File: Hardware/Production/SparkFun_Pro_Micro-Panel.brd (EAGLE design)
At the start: 103.6 x 148.6 mm, 1548 parts, among them J1 Qwiic, J13 Qwiic, J17 Qwiic, J2 Qwiic, J21 Qwiic, J25 Qwiic, J29 Qwiic, J33 Qwiic, J37 Qwiic, J41 Qwiic, J45 Qwiic, J49 Qwiic, J53 Qwiic, J57 Qwiic, J9 Qwiic, U1 3.3V, U10 3.3V, U11 ATmega32U4, U12 3.3V, U13 ATmega32U4, U14 3.3V, U15 ATmega32U4, U16 3.3V, U17 ATmega32U4, U18 3.3V, U19 ATmega32U4, U2 ATmega32U4, U20 3.3V, U21 ATmega32U4, U22 3.3V, U23 ATmega32U4, U24 3.3V, U25 ATmega32U4, U26 3.3V, U27 ATmega32U4, U28 3.3V, U29 ATmega32U4, U3 ATmega32U4, U30 3.3V, U4 3.3V, U5 ATmega32U4, U6 3.3V, U7 ATmega32U4, U8 3.3V, U9 ATmega32U4, Y1 32MHz, Y10 32MHz, Y11 32MHz, Y12 32MHz, Y13 32MHz, Y14 32MHz, Y15 32MHz, Y2 32MHz, Y3 32MHz, Y4 32MHz, Y5 32MHz, Y6 32MHz, Y7 32MHz, Y8 32MHz, Y9 32MHz

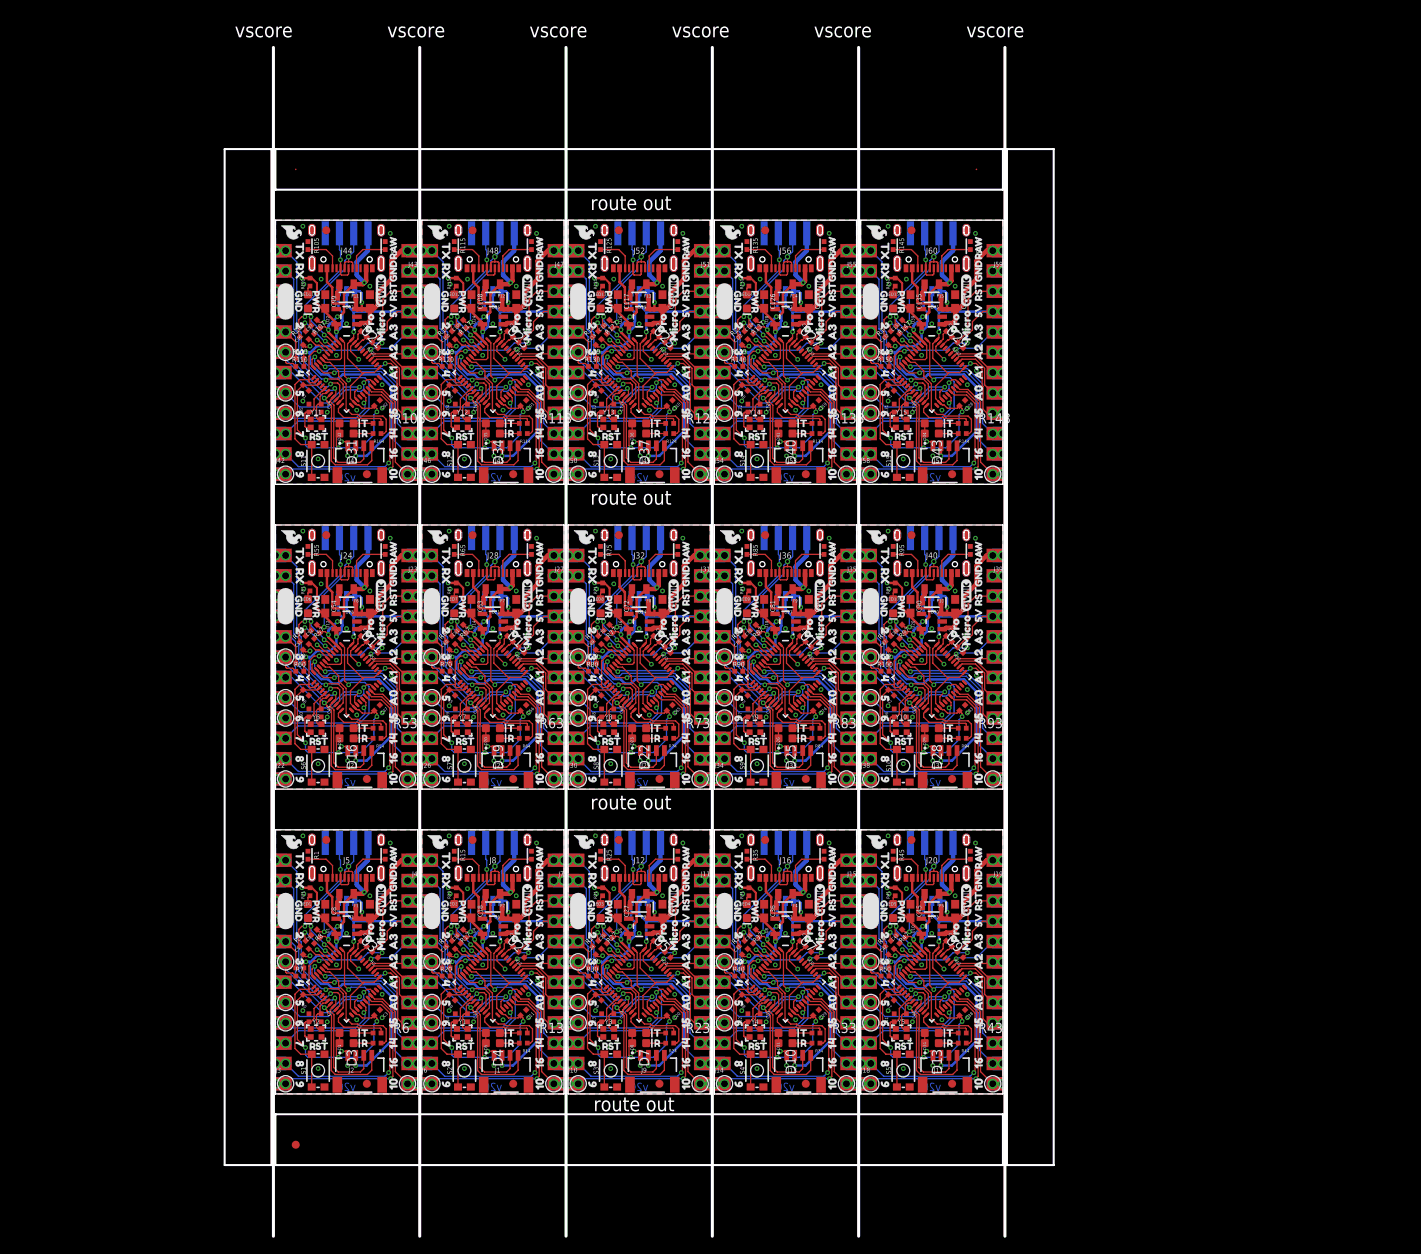
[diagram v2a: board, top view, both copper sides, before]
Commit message: Red boards ordered
Modify castellated 1x12 to larger diameter plated castellated holes. Panelize with route-out around castellated edges. Scoot Qwiic connector in to use that side of the board as the tab.
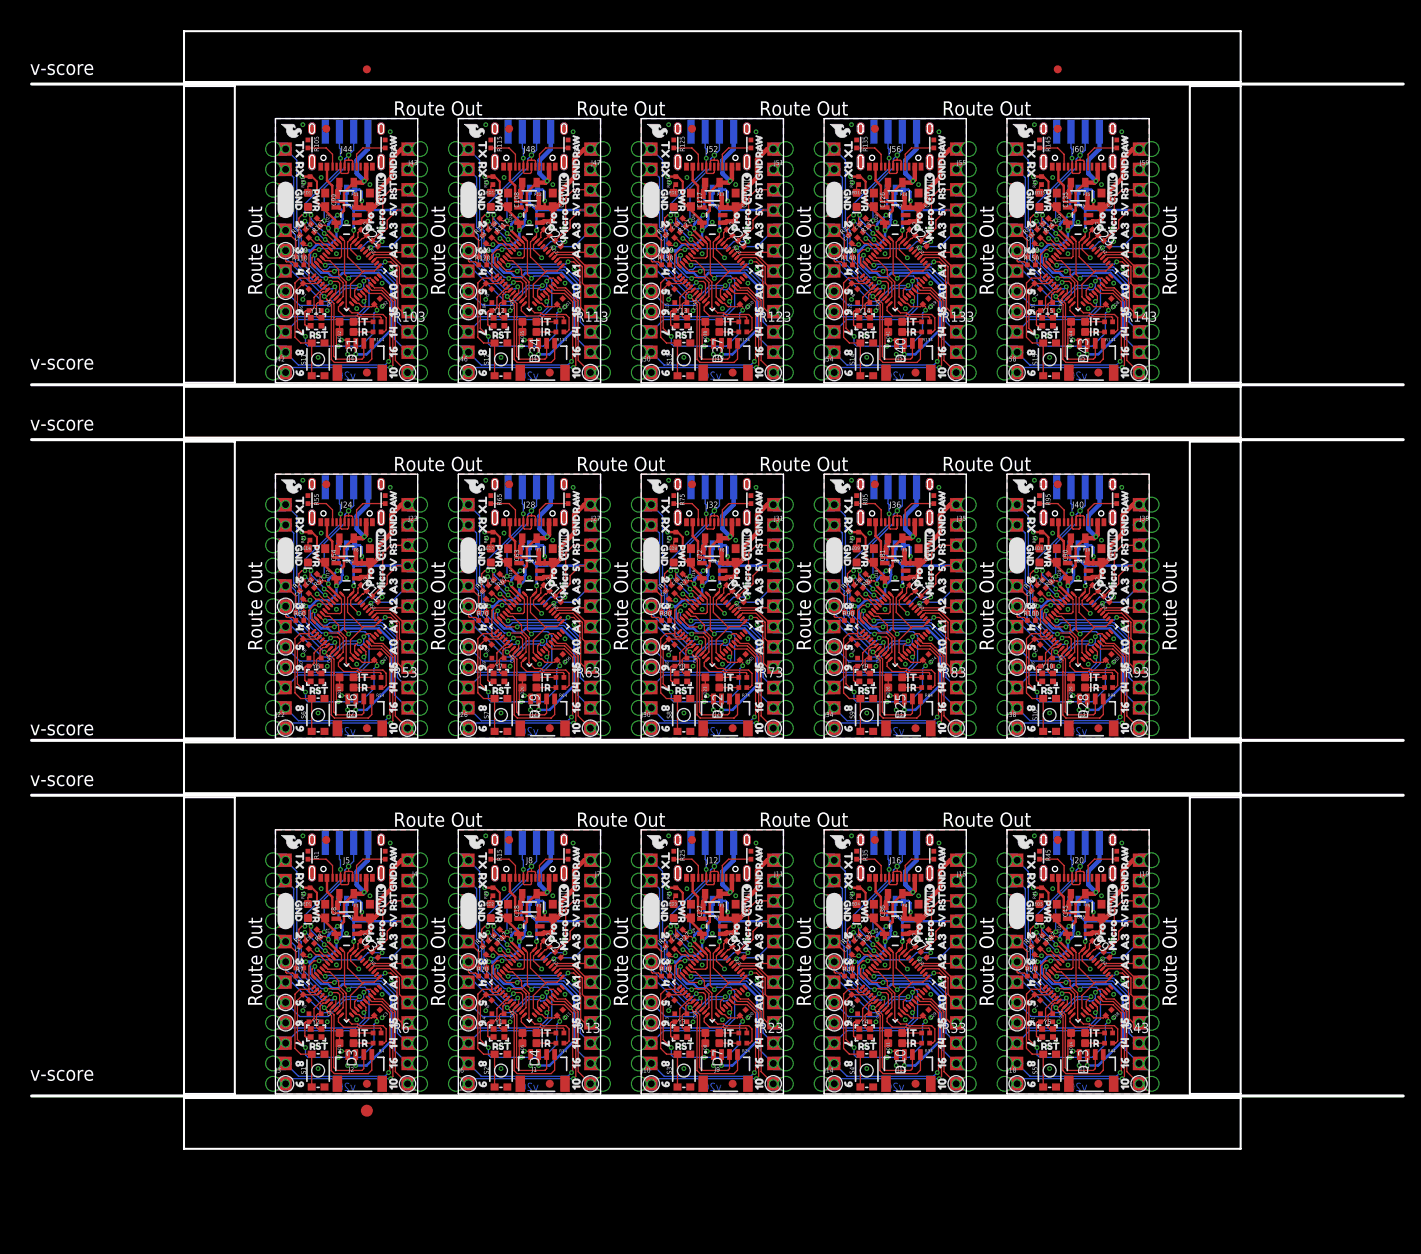
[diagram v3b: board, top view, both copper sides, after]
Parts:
- E$2: device SparkFun-Aesthetics:FIDUCIAL-0.2MM -> SparkFun-Aesthetics:FIDUCIAL-1X2
- E$3: device SparkFun-Aesthetics:FIDUCIAL-0.2MM -> SparkFun-Retired:FIDUCIAL-1.5X3
- moved E$3 140.2 mm to (11.4, -2.10)
- moved E$1 134.7 mm to (11.4, 128.1)
- moved E$2 96.1 mm to (97.8, 128.1)
- moved J57 22.3 mm to (102.0, 93.8)
- moved C129 22.3 mm to (102.5, 107.7)
- moved C133 22.3 mm to (96.6, 108.1)
- moved C134 22.3 mm to (103.3, 111.8)
- moved JP57 22.3 mm to (102.9, 90.2)
- moved JP58 22.3 mm to (97.8, 120.7)
- moved LED15 22.3 mm to (95.5, 111.8)
- moved R145 22.3 mm to (95.5, 118.7)
- moved R146 22.3 mm to (105.2, 118.7)
- moved R147 22.3 mm to (96.3, 109.1)
- moved U$888 22.3 mm to (103.3, 106.9)
- moved U$903 22.3 mm to (94.4, 114.0)
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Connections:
- new net 3.3V12: C117.2, J49.2, JP52.1, R121.2, R129.2, R130.2, U26.5
- new net 3.3V13: C126.2, J53.2, JP56.1, R131.2, R139.2, R140.2, U28.5
- new net 3.3V14: C135.2, J57.2, JP60.1, R141.2, R149.2, R150.2, U30.5
- new net 3.3V2: C27.2, J9.2, JP11.1, R21.2, R29.2, R30.2, U6.5
- new net 3.3V3: C36.2, J13.2, JP16.1, R31.2, R39.2, R40.2, U8.5
- new net 3.3V4: C45.2, J17.2, JP20.1, R41.2, R49.2, R50.2, U10.5
- new net 3.3V7: C72.2, J29.2, JP32.1, R71.2, R79.2, R80.2, U16.5
- new net 3.3V8: C81.2, J33.2, JP36.1, R81.2, R89.2, R90.2, U18.5
- new net 3.3V9: C90.2, J37.2, JP40.1, R100.2, R91.2, R99.2, U20.5
- new net A10: J11.7, J11.7B, U5.37
- new net A11: J11.8, J11.8B, U5.36
- new net A12: J15.5, J15.5B, U7.39
- new net A13: J15.6, J15.6B, U7.38
- new net A14: J15.7, J15.7B, U7.37
- new net A15: J15.8, J15.8B, U7.36
- new net A16: J19.5, J19.5B, U9.39
- new net A17: J19.6, J19.6B, U9.38
- new net A18: J19.7, J19.7B, U9.37
- new net A19: J19.8, J19.8B, U9.36
- new net A28: J31.5, J31.5B, U15.39
- new net A29: J31.6, J31.6B, U15.38
- new net A30: J31.7, J31.7B, U15.37
- new net A31: J31.8, J31.8B, U15.36
- new net A32: J35.5, J35.5B, U17.39
- new net A33: J35.6, J35.6B, U17.38
- new net A34: J35.7, J35.7B, U17.37
- new net A35: J35.8, J35.8B, U17.36
- new net A36: J39.5, J39.5B, U19.39
- new net A37: J39.6, J39.6B, U19.38
- new net A38: J39.7, J39.7B, U19.37
- new net A39: J39.8, J39.8B, U19.36
- new net A48: J51.5, J51.5B, U25.39
- new net A49: J51.6, J51.6B, U25.38
- new net A50: J51.7, J51.7B, U25.37
- new net A51: J51.8, J51.8B, U25.36
- new net A52: J55.5, J55.5B, U27.39
- new net A53: J55.6, J55.6B, U27.38
- new net A54: J55.7, J55.7B, U27.37
- new net A55: J55.8, J55.8B, U27.36
- new net A56: J59.5, J59.5B, U29.39
- new net A57: J59.6, J59.6B, U29.38
- new net A58: J59.7, J59.7B, U29.37
- new net A59: J59.8, J59.8B, U29.36
- new net A8: J11.5, J11.5B, U5.39
- new net A9: J11.6, J11.6B, U5.38
- new net AREF12: C111.2, U25.42
- new net AREF13: C120.2, U27.42
- new net AREF14: C129.2, U29.42
- new net AREF2: C21.2, U5.42
- new net AREF3: C30.2, U7.42
- new net AREF4: C39.2, U9.42
- new net AREF7: C66.2, U15.42
- new net AREF8: C75.2, U17.42
- new net AREF9: C84.2, U19.42
- new net D+12: R128.2, U25.4
- new net D+13: R138.2, U27.4
- new net D+14: R148.2, U29.4
- new net D+2: R28.2, U5.4
- new net D+3: R38.2, U7.4
- new net D+4: R48.2, U9.4
- new net D+7: R78.2, U15.4
- new net D+8: R88.2, U17.4
- new net D+9: R98.2, U19.4
- new net D-12: R127.2, U25.3
- new net D-13: R137.2, U27.3
- new net D-14: R147.2, U29.3
- new net D-2: R27.2, U5.3
- new net D-3: R37.2, U7.3
- new net D-4: R47.2, U9.3
- new net D-7: R77.2, U15.3
- new net D-8: R87.2, U17.3
- new net D-9: R97.2, U19.3
- new net D-_HV12: J52.A7, J52.B7, JP51.D-, R127.1
- new net D-_HV13: J56.A7, J56.B7, JP55.D-, R137.1
- new net D-_HV14: J60.A7, J60.B7, JP59.D-, R147.1
- new net D-_HV2: J12.A7, J12.B7, JP10.D-, R27.1
- new net D-_HV3: J16.A7, J16.B7, JP15.D-, R37.1
- new net D-_HV4: J20.A7, J20.B7, JP19.D-, R47.1
- new net D-_HV7: J32.A7, J32.B7, JP31.D-, R77.1
- new net D-_HV8: J36.A7, J36.B7, JP35.D-, R87.1
- new net D-_HV9: J40.A7, J40.B7, JP39.D-, R97.1
- new net D100: J58.2, J58.2B, U29.28
- new net D101: J58.6, J58.6B, U29.25
- new net D102: J58.5, J58.5B, U29.31
- new net D103: J58.4, J58.4B, U29.27
- new net D104: J58.3, J58.3B, U29.1
- new net D105: J59.12, J59.12B, U29.30
- new net D15: J10.1, J10.1B, U5.29
- new net D16: J10.2, J10.2B, U5.28
- new net D17: J10.6, J10.6B, U5.25
- new net D18: J10.5, J10.5B, U5.31
- new net D19: J10.4, J10.4B, U5.27
- new net D2/SDA12: J49.3, J50.8, J50.8B, R129.1, U25.19
- new net D2/SDA13: J53.3, J54.8, J54.8B, R139.1, U27.19
- new net D2/SDA14: J57.3, J58.8, J58.8B, R149.1, U29.19
- new net D2/SDA2: J10.8, J10.8B, J9.3, R29.1, U5.19
- new net D2/SDA3: J13.3, J14.8, J14.8B, R39.1, U7.19
- new net D2/SDA4: J17.3, J18.8, J18.8B, R49.1, U9.19
- new net D2/SDA7: J29.3, J30.8, J30.8B, R79.1, U15.19
- new net D2/SDA8: J33.3, J34.8, J34.8B, R89.1, U17.19
- new net D2/SDA9: J37.3, J38.8, J38.8B, R99.1, U19.19
- new net D20: J10.3, J10.3B, U5.1
- new net D21: J11.12, J11.12B, U5.30
- new net D22: J14.1, J14.1B, U7.29
- new net D23: J14.2, J14.2B, U7.28
- new net D24: J14.6, J14.6B, U7.25
- new net D25: J14.5, J14.5B, U7.31
- new net D26: J14.4, J14.4B, U7.27
- new net D27: J14.3, J14.3B, U7.1
- new net D28: J15.12, J15.12B, U7.30
- new net D29: J18.1, J18.1B, U9.29
- new net D3/SCL12: J49.4, J50.7, J50.7B, R130.1, U25.18
- new net D3/SCL13: J53.4, J54.7, J54.7B, R140.1, U27.18
- new net D3/SCL14: J57.4, J58.7, J58.7B, R150.1, U29.18
- new net D3/SCL2: J10.7, J10.7B, J9.4, R30.1, U5.18
- new net D3/SCL3: J13.4, J14.7, J14.7B, R40.1, U7.18
- new net D3/SCL4: J17.4, J18.7, J18.7B, R50.1, U9.18
- new net D3/SCL7: J29.4, J30.7, J30.7B, R80.1, U15.18
- new net D3/SCL8: J33.4, J34.7, J34.7B, R90.1, U17.18
- new net D3/SCL9: J37.4, J38.7, J38.7B, R100.1, U19.18
- new net D30: J18.2, J18.2B, U9.28
- new net D31: J18.6, J18.6B, U9.25
- new net D32: J18.5, J18.5B, U9.31
- new net D33: J18.4, J18.4B, U9.27
- new net D34: J18.3, J18.3B, U9.1
- new net D35: J19.12, J19.12B, U9.30
- new net D50: J30.1, J30.1B, U15.29
- new net D51: J30.2, J30.2B, U15.28
- new net D52: J30.6, J30.6B, U15.25
- new net D53: J30.5, J30.5B, U15.31
- new net D54: J30.4, J30.4B, U15.27
- new net D55: J30.3, J30.3B, U15.1
- new net D56: J31.12, J31.12B, U15.30
- new net D57: J34.1, J34.1B, U17.29
- new net D58: J34.2, J34.2B, U17.28
- new net D59: J34.6, J34.6B, U17.25
- new net D60: J34.5, J34.5B, U17.31
- new net D61: J34.4, J34.4B, U17.27
- new net D62: J34.3, J34.3B, U17.1
- new net D63: J35.12, J35.12B, U17.30
- new net D64: J38.1, J38.1B, U19.29
- new net D65: J38.2, J38.2B, U19.28
- new net D66: J38.6, J38.6B, U19.25
- new net D67: J38.5, J38.5B, U19.31
- new net D68: J38.4, J38.4B, U19.27
- new net D69: J38.3, J38.3B, U19.1
- new net D70: J39.12, J39.12B, U19.30
- new net D85: J50.1, J50.1B, U25.29
- new net D86: J50.2, J50.2B, U25.28
- new net D87: J50.6, J50.6B, U25.25
- new net D88: J50.5, J50.5B, U25.31
- new net D89: J50.4, J50.4B, U25.27
- new net D90: J50.3, J50.3B, U25.1
- new net D91: J51.12, J51.12B, U25.30
- new net D92: J54.1, J54.1B, U27.29
- new net D93: J54.2, J54.2B, U27.28
- new net D94: J54.6, J54.6B, U27.25
- new net D95: J54.5, J54.5B, U27.31
- new net D96: J54.4, J54.4B, U27.27
- new net D97: J54.3, J54.3B, U27.1
- new net D98: J55.12, J55.12B, U27.30
- new net D99: J58.1, J58.1B, U29.29
- new net DP_HV12: J52.A6, J52.B6, JP51.D+, R128.1
- new net DP_HV13: J56.A6, J56.B6, JP55.D+, R138.1
- new net DP_HV14: J60.A6, J60.B6, JP59.D+, R148.1
- new net DP_HV2: J12.A6, J12.B6, JP10.D+, R28.1
- new net DP_HV3: J16.A6, J16.B6, JP15.D+, R38.1
- new net DP_HV4: J20.A6, J20.B6, JP19.D+, R48.1
- new net DP_HV7: J32.A6, J32.B6, JP31.D+, R78.1
- new net DP_HV8: J36.A6, J36.B6, JP35.D+, R88.1
- new net DP_HV9: J40.A6, J40.B6, JP39.D+, R98.1
- new net GND12: C109.1, C110.1, C111.1, C112.2, C113.2, C114.1, C115.1, C116.1, C117.1, J49.1, J50.10, J50.10B, J50.9, J50.9B, J51.2, J51.2B, J52.GND, J52.GND2, JP51.GND, LED13.C, R125.1, R126.1, S13.1, S13.2, U25.15, U25.23, U25.33, U25.35, U25.43, U25.5, U26.2
- new net GND13: C118.1, C119.1, C120.1, C121.2, C122.2, C123.1, C124.1, C125.1, C126.1, J53.1, J54.10, J54.10B, J54.9, J54.9B, J55.2, J55.2B, J56.GND, J56.GND2, JP55.GND, LED14.C, R135.1, R136.1, S14.1, S14.2, U27.15, U27.23, U27.33, U27.35, U27.43, U27.5, U28.2
- new net GND14: C127.1, C128.1, C129.1, C130.2, C131.2, C132.1, C133.1, C134.1, C135.1, J57.1, J58.10, J58.10B, J58.9, J58.9B, J59.2, J59.2B, J60.GND, J60.GND2, JP59.GND, LED15.C, R145.1, R146.1, S15.1, S15.2, U29.15, U29.23, U29.33, U29.35, U29.43, U29.5, U30.2
- new net GND2: C19.1, C20.1, C21.1, C22.2, C23.2, C24.1, C25.1, C26.1, C27.1, J10.10, J10.10B, J10.9, J10.9B, J11.2, J11.2B, J12.GND, J12.GND2, J9.1, JP10.GND, LED3.C, R25.1, R26.1, S3.1, S3.2, U5.15, U5.23, U5.33, U5.35, U5.43, U5.5, U6.2
- new net GND3: C28.1, C29.1, C30.1, C31.2, C32.2, C33.1, C34.1, C35.1, C36.1, J13.1, J14.10, J14.10B, J14.9, J14.9B, J15.2, J15.2B, J16.GND, J16.GND2, JP15.GND, LED4.C, R35.1, R36.1, S4.1, S4.2, U7.15, U7.23, U7.33, U7.35, U7.43, U7.5, U8.2
- new net GND4: C37.1, C38.1, C39.1, C40.2, C41.2, C42.1, C43.1, C44.1, C45.1, J17.1, J18.10, J18.10B, J18.9, J18.9B, J19.2, J19.2B, J20.GND, J20.GND2, JP19.GND, LED5.C, R45.1, R46.1, S5.1, S5.2, U10.2, U9.15, U9.23, U9.33, U9.35, U9.43, U9.5
- new net GND7: C64.1, C65.1, C66.1, C67.2, C68.2, C69.1, C70.1, C71.1, C72.1, J29.1, J30.10, J30.10B, J30.9, J30.9B, J31.2, J31.2B, J32.GND, J32.GND2, JP31.GND, LED8.C, R75.1, R76.1, S8.1, S8.2, U15.15, U15.23, U15.33, U15.35, U15.43, U15.5, U16.2
- new net GND8: C73.1, C74.1, C75.1, C76.2, C77.2, C78.1, C79.1, C80.1, C81.1, J33.1, J34.10, J34.10B, J34.9, J34.9B, J35.2, J35.2B, J36.GND, J36.GND2, JP35.GND, LED9.C, R85.1, R86.1, S9.1, S9.2, U17.15, U17.23, U17.33, U17.35, U17.43, U17.5, U18.2
- new net GND9: C82.1, C83.1, C84.1, C85.2, C86.2, C87.1, C88.1, C89.1, C90.1, J37.1, J38.10, J38.10B, J38.9, J38.9B, J39.2, J39.2B, J40.GND, J40.GND2, JP39.GND, LED10.C, R95.1, R96.1, S10.1, S10.2, U19.15, U19.23, U19.33, U19.35, U19.43, U19.5, U20.2
- new net MISO12: J51.10, J51.10B, U25.11
- new net MISO13: J55.10, J55.10B, U27.11
- new net MISO14: J59.10, J59.10B, U29.11
- new net MISO2: J11.10, J11.10B, U5.11
- new net MISO3: J15.10, J15.10B, U7.11
- new net MISO4: J19.10, J19.10B, U9.11
- new net MISO7: J31.10, J31.10B, U15.11
- new net MISO8: J35.10, J35.10B, U17.11
- new net MISO9: J39.10, J39.10B, U19.11
- new net MOSI12: J51.11, J51.11B, U25.10
- new net MOSI13: J55.11, J55.11B, U27.10
- new net MOSI14: J59.11, J59.11B, U29.10
- new net MOSI2: J11.11, J11.11B, U5.10
- new net MOSI3: J15.11, J15.11B, U7.10
- new net MOSI4: J19.11, J19.11B, U9.10
- new net MOSI7: J31.11, J31.11B, U15.10
- new net MOSI8: J35.11, J35.11B, U17.10
- new net MOSI9: J39.11, J39.11B, U19.10
- new net N$100: C131.1, U29.16, Y15.1
- new net N$101: C130.1, U29.17, Y15.3
- new net N$102: D44.C, R144.2
- new net N$103: D43.C, R143.2
- new net N$104: J60.A5, R146.2
- new net N$105: J60.B5, R145.2
- new net N$14: LED3.A, R21.1
- new net N$15: C23.1, U5.16, Y3.1
- new net N$16: C22.1, U5.17, Y3.3
- new net N$17: D8.C, R24.2
- new net N$18: D7.C, R23.2
- new net N$19: J12.A5, R26.2
- new net N$20: J12.B5, R25.2
- new net N$21: LED4.A, R31.1
- new net N$22: C32.1, U7.16, Y4.1
- new net N$23: C31.1, U7.17, Y4.3
- new net N$24: D11.C, R34.2
- new net N$25: D10.C, R33.2
- new net N$26: J16.A5, R36.2
- new net N$27: J16.B5, R35.2
- new net N$28: LED5.A, R41.1
- new net N$29: C41.1, U9.16, Y5.1
- new net N$30: C40.1, U9.17, Y5.3
- new net N$31: D14.C, R44.2
- new net N$32: D13.C, R43.2
- new net N$33: J20.A5, R46.2
- new net N$34: J20.B5, R45.2
- new net N$50: LED8.A, R71.1
- new net N$51: C68.1, U15.16, Y8.1
- new net N$52: C67.1, U15.17, Y8.3
- new net N$53: D23.C, R74.2
- new net N$54: D22.C, R73.2
- new net N$55: J32.A5, R76.2
- new net N$56: J32.B5, R75.2
- new net N$57: LED9.A, R81.1
- new net N$58: C77.1, U17.16, Y9.1
- new net N$59: C76.1, U17.17, Y9.3
- new net N$60: D26.C, R84.2
- new net N$61: D25.C, R83.2
- new net N$62: J36.A5, R86.2
- new net N$63: J36.B5, R85.2
- new net N$64: LED10.A, R91.1
- new net N$65: C86.1, U19.16, Y10.1
- new net N$66: C85.1, U19.17, Y10.3
- new net N$67: D29.C, R94.2
- new net N$68: D28.C, R93.2
- new net N$69: J40.A5, R96.2
- new net N$70: J40.B5, R95.2
- new net N$85: LED13.A, R121.1
- new net N$86: C113.1, U25.16, Y13.1
- new net N$87: C112.1, U25.17, Y13.3
- new net N$88: D38.C, R124.2
- new net N$89: D37.C, R123.2
- new net N$90: J52.A5, R126.2
- new net N$91: J52.B5, R125.2
- new net N$92: LED14.A, R131.1
- new net N$93: C122.1, U27.16, Y14.1
- new net N$94: C121.1, U27.17, Y14.3
- new net N$95: D41.C, R134.2
- new net N$96: D40.C, R133.2
- new net N$97: J56.A5, R136.2
- new net N$98: J56.B5, R135.2
- new net N$99: LED15.A, R141.1
- new net RAW12: C116.2, D39.C, J51.1, J51.1B, JP52.3, U26.1, U26.3
- new net RAW13: C125.2, D42.C, J55.1, J55.1B, JP56.3, U28.1, U28.3
- new net RAW14: C134.2, D45.C, J59.1, J59.1B, JP60.3, U30.1, U30.3
- new net RAW2: C26.2, D9.C, J11.1, J11.1B, JP11.3, U6.1, U6.3
- new net RAW3: C35.2, D12.C, J15.1, J15.1B, JP16.3, U8.1, U8.3
- new net RAW4: C44.2, D15.C, J19.1, J19.1B, JP20.3, U10.1, U10.3
- new net RAW7: C71.2, D24.C, J31.1, J31.1B, JP32.3, U16.1, U16.3
- new net RAW8: C80.2, D27.C, J35.1, J35.1B, JP36.3, U18.1, U18.3
- new net RAW9: C89.2, D30.C, J39.1, J39.1B, JP40.3, U20.1, U20.3
- new net RESET12: J51.3, J51.3B, R122.1, S13.3, S13.4, U25.13
- new net RESET13: J55.3, J55.3B, R132.1, S14.3, S14.4, U27.13
- new net RESET14: J59.3, J59.3B, R142.1, S15.3, S15.4, U29.13
- new net RESET2: J11.3, J11.3B, R22.1, S3.3, S3.4, U5.13
- new net RESET3: J15.3, J15.3B, R32.1, S4.3, S4.4, U7.13
- new net RESET4: J19.3, J19.3B, R42.1, S5.3, S5.4, U9.13
- new net RESET7: J31.3, J31.3B, R72.1, S8.3, S8.4, U15.13
- new net RESET8: J35.3, J35.3B, R82.1, S9.3, S9.4, U17.13
- new net RESET9: J39.3, J39.3B, R92.1, S10.3, S10.4, U19.13
- new net RXI12: J50.11, J50.11B, U25.20
- new net RXI13: J54.11, J54.11B, U27.20
- new net RXI14: J58.11, J58.11B, U29.20
- new net RXI2: J10.11, J10.11B, U5.20
- new net RXI3: J14.11, J14.11B, U7.20
- new net RXI4: J18.11, J18.11B, U9.20
- new net RXI7: J30.11, J30.11B, U15.20
- new net RXI8: J34.11, J34.11B, U17.20
- new net RXI9: J38.11, J38.11B, U19.20
- new net RXLED12: R124.1, U25.8
- new net RXLED13: R134.1, U27.8
- new net RXLED14: R144.1, U29.8
- new net RXLED2: R24.1, U5.8
- new net RXLED3: R34.1, U7.8
- new net RXLED4: R44.1, U9.8
- new net RXLED7: R74.1, U15.8
- new net RXLED8: R84.1, U17.8
- new net RXLED9: R94.1, U19.8
- new net SCK12: J51.9, J51.9B, U25.9
- new net SCK13: J55.9, J55.9B, U27.9
- new net SCK14: J59.9, J59.9B, U29.9
- new net SCK2: J11.9, J11.9B, U5.9
- new net SCK3: J15.9, J15.9B, U7.9
- new net SCK4: J19.9, J19.9B, U9.9
- new net SCK7: J31.9, J31.9B, U15.9
- new net SCK8: J35.9, J35.9B, U17.9
- new net SCK9: J39.9, J39.9B, U19.9
- new net TXLED12: R123.1, U25.22
- new net TXLED13: R133.1, U27.22
- new net TXLED14: R143.1, U29.22
- new net TXLED2: R23.1, U5.22
- new net TXLED3: R33.1, U7.22
- new net TXLED4: R43.1, U9.22
- new net TXLED7: R73.1, U15.22
- new net TXLED8: R83.1, U17.22
- new net TXLED9: R93.1, U19.22
- new net TXO12: J50.12, J50.12B, U25.21
- new net TXO13: J54.12, J54.12B, U27.21
- new net TXO14: J58.12, J58.12B, U29.21
- new net TXO2: J10.12, J10.12B, U5.21
- new net TXO3: J14.12, J14.12B, U7.21
- new net TXO4: J18.12, J18.12B, U9.21
- new net TXO7: J30.12, J30.12B, U15.21
- new net TXO8: J34.12, J34.12B, U17.21
- new net TXO9: J38.12, J38.12B, U19.21
- new net UCAP12: C114.2, U25.6
- new net UCAP13: C123.2, U27.6
- new net UCAP14: C132.2, U29.6
- new net UCAP2: C24.2, U5.6
- new net UCAP3: C33.2, U7.6
- new net UCAP4: C42.2, U9.6
- new net UCAP7: C69.2, U15.6
- new net UCAP8: C78.2, U17.6
- new net UCAP9: C87.2, U19.6
- new net USB_RAW12: D39.A, F13.2
- new net USB_RAW13: D42.A, F14.2
- new net USB_RAW14: D45.A, F15.2
- new net USB_RAW2: D9.A, F3.2
- new net USB_RAW3: D12.A, F4.2
- new net USB_RAW4: D15.A, F5.2
- new net USB_RAW7: D24.A, F8.2
- new net USB_RAW8: D27.A, F9.2
- new net USB_RAW9: D30.A, F10.2
- new net VCC12: C109.2, C110.2, D37.A, D38.A, J51.4, J51.4B, JP52.2, R122.2, U25.14, U25.24, U25.34, U25.44
- new net VCC13: C118.2, C119.2, D40.A, D41.A, J55.4, J55.4B, JP56.2, R132.2, U27.14, U27.24, U27.34, U27.44
- new net VCC14: C127.2, C128.2, D43.A, D44.A, J59.4, J59.4B, JP60.2, R142.2, U29.14, U29.24, U29.34, U29.44
- new net VCC2: C19.2, C20.2, D7.A, D8.A, J11.4, J11.4B, JP11.2, R22.2, U5.14, U5.24, U5.34, U5.44
- new net VCC3: C28.2, C29.2, D10.A, D11.A, J15.4, J15.4B, JP16.2, R32.2, U7.14, U7.24, U7.34, U7.44
- new net VCC4: C37.2, C38.2, D13.A, D14.A, J19.4, J19.4B, JP20.2, R42.2, U9.14, U9.24, U9.34, U9.44
- new net VCC7: C64.2, C65.2, D22.A, D23.A, J31.4, J31.4B, JP32.2, R72.2, U15.14, U15.24, U15.34, U15.44
- new net VCC8: C73.2, C74.2, D25.A, D26.A, J35.4, J35.4B, JP36.2, R82.2, U17.14, U17.24, U17.34, U17.44
- new net VCC9: C82.2, C83.2, D28.A, D29.A, J39.4, J39.4B, JP40.2, R92.2, U19.14, U19.24, U19.34, U19.44
- new net V_USB12: C115.2, F13.1, J52.VBUS1, J52.VBUS2, JP51.VBUS, U25.2, U25.7
- new net V_USB13: C124.2, F14.1, J56.VBUS1, J56.VBUS2, JP55.VBUS, U27.2, U27.7
- new net V_USB14: C133.2, F15.1, J60.VBUS1, J60.VBUS2, JP59.VBUS, U29.2, U29.7
- new net V_USB2: C25.2, F3.1, J12.VBUS1, J12.VBUS2, JP10.VBUS, U5.2, U5.7
- new net V_USB3: C34.2, F4.1, J16.VBUS1, J16.VBUS2, JP15.VBUS, U7.2, U7.7
- new net V_USB4: C43.2, F5.1, J20.VBUS1, J20.VBUS2, JP19.VBUS, U9.2, U9.7
- new net V_USB7: C70.2, F8.1, J32.VBUS1, J32.VBUS2, JP31.VBUS, U15.2, U15.7
- new net V_USB8: C79.2, F9.1, J36.VBUS1, J36.VBUS2, JP35.VBUS, U17.2, U17.7
- new net V_USB9: C88.2, F10.1, J40.VBUS1, J40.VBUS2, JP39.VBUS, U19.2, U19.7
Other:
- board size 103.6 x 148.6 mm -> 171.4 x 139.7 mm
- board text added: "Route Out"
- board text added: "v-score"
- board text removed: "route out"
- board text removed: "vscore"
